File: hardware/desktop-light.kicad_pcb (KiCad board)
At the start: 2 copper layers, 100 x 100 mm, 95 parts, among them J1 Conn_01x06, J2 Conn_01x06, J3 USB_B_Micro, J4 Barrel_Jack, J5 Conn_01x06, Q1 BSS138, Q2 BSS138, U1 ESP32-WROOM-32, U2 AMS1117-3.3, U3 CH340C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

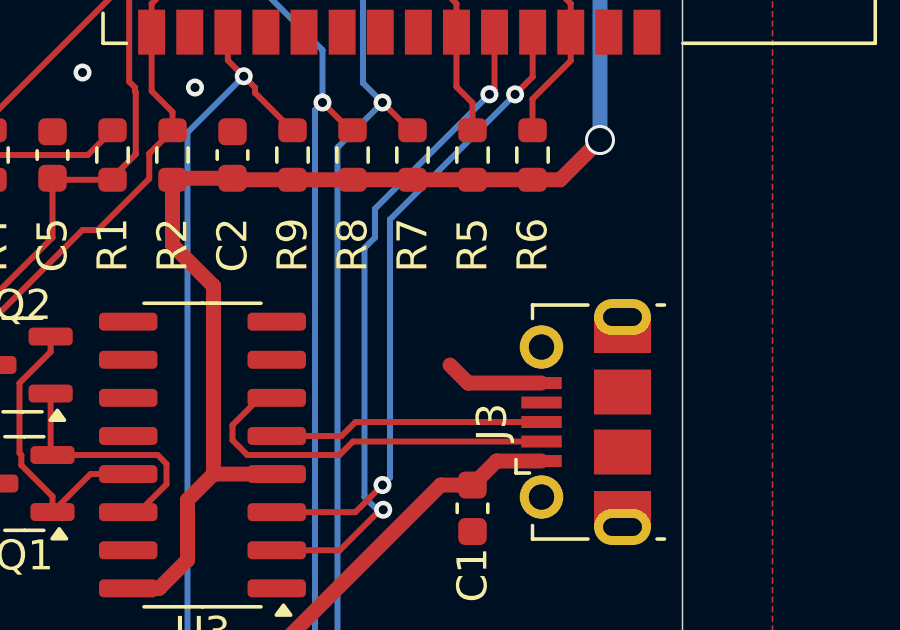
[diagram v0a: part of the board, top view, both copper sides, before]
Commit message: add vias
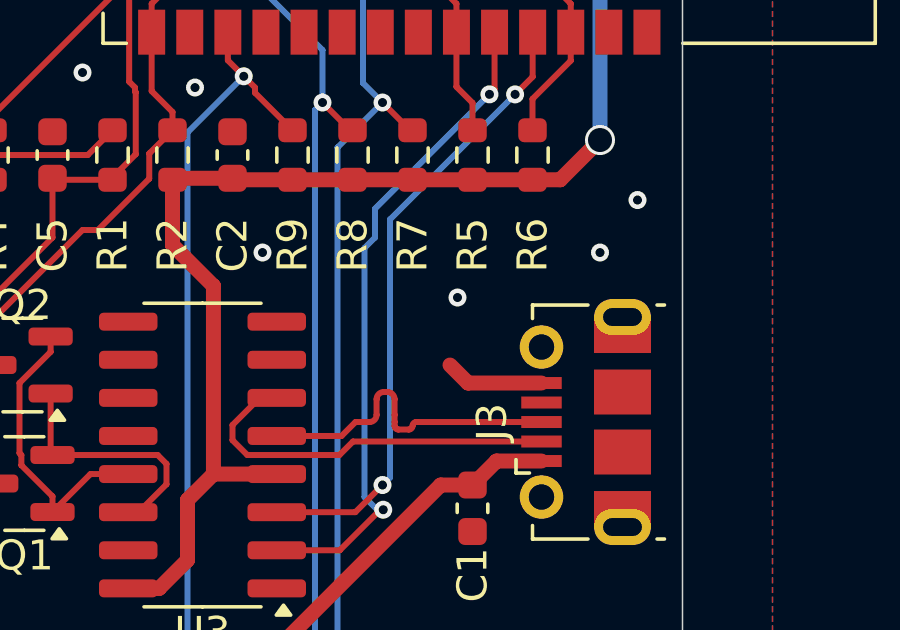
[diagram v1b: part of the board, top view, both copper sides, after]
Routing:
- net D+: track 9.02 -> 11.0 mm
- net GND: vias 61 -> 65

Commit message: add real photos
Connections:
- U1 pad 28: unconnected-(U1-IO17-Pad28) -> DIN
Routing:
- net DIN: track 0.00 -> 29.0 mm, vias 0 -> 1
